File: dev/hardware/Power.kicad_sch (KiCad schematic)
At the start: 7 parts, among them J301 DC IN, Q301 IPP80P03P4L-04, U301 LF33_TO220

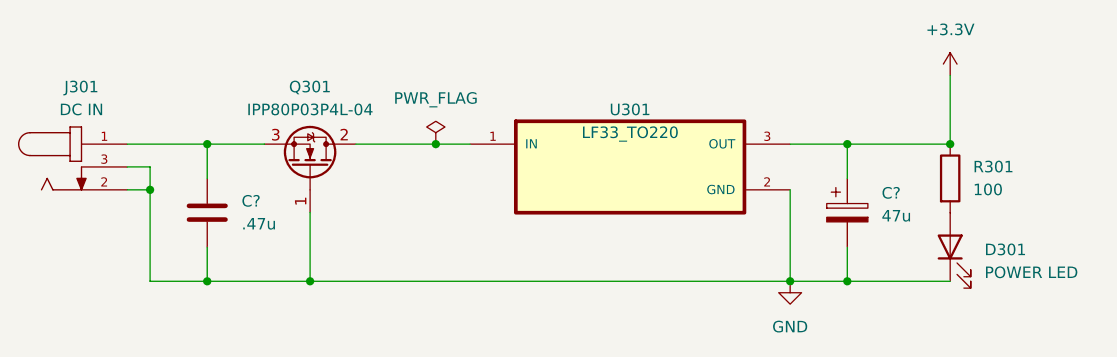
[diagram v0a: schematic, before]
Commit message: Finalized dev PCB for 1st run
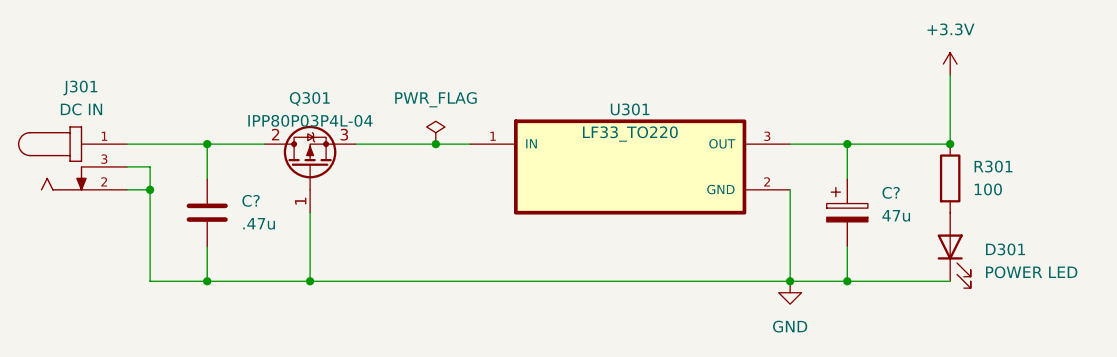
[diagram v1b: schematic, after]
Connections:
- net at C?.2, J301.1: now also Q301.2 (D); no longer Q301.3 (S)
- net at U301.1 (IN): now also Q301.3 (S); no longer Q301.2 (D)
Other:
- moved on the sheet: Q301
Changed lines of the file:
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@@
     )
   )
-  (symbol (lib_id "jcap-symbols:IPP80P03P4L-04") (at 120.65 90.17 270) (mirror x) (unit 1)
+  (symbol (lib_id "jcap-symbols:IPP80P03P4L-04") (at 120.65 91.44 90) (unit 1)
     (in_bom yes) (on_board yes) (dnp no)
-    (property "Reference" "Q301" (at 120.65 81.28 90)
+    (property "Reference" "Q301" (at 120.65 82.55 90)
       (effects (font (size 1.27 1.27)))
     )
-    (property "Value" "IPP80P03P4L-04" (at 120.65 83.82 90)
+    (property "Value" "IPP80P03P4L-04" (at 120.65 85.09 90)
       (effects (font (size 1.27 1.27)))
     )
-    (property "Footprint" "Package_TO_SOT_THT:TO-220-3_Horizontal_TabDown" (at 118.745 83.82 0)
+    (property "Footprint" "Package_TO_SOT_THT:TO-220-3_Horizontal_TabDown" (at 122.555 85.09 0)
       (effects (font (size 1.27 1.27) italic) (justify left) hide)
     )
-    (property "Datasheet" "https://www.infineon.com/dgdl/Infineon-I80P03P4L_04-DataSheet-v01_01-EN.pdf?fileId=db3a30431ddc9372011e07e95eb827d7" (at 120.65 90.17 0)
+    (property "Datasheet" "https://www.infineon.com/dgdl/Infineon-I80P03P4L_04-DataSheet-v01_01-EN.pdf?fileId=db3a30431ddc9372011e07e95eb827d7" (at 120.65 91.44 0)
       (effects (font (size 1.27 1.27)) (justify left) hide)
     )

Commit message: Finalized dev board administrivia
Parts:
- C?: Part (none) -> C330C474K5R5TA
- C?: Part (none) -> EEU-FR1J470
- D301: Part (none) -> HLMP-1790
- J301: Part (none) -> PJ-202AH
- Q301: Part (none) -> IPP80P03P4L04AKSA2
- R301: Part (none) -> CF12JT100R
- U301: value LF33_TO220 -> LM3940IT; Part (none) -> LM3940IT-3.3/NOPB
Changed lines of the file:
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@@
       (effects (font (size 1.27 1.27)) (justify bottom) hide)
     )
-    (property "Datasheet" "~" (at 95.25 90.17 0)
+    (property "Datasheet" "https://www.cuidevices.com/product/resource/pj-202ah.pdf" (at 95.25 90.17 0)
+      (effects (font (size 1.27 1.27)) hide)
+    )
+    (property "Part" "PJ-202AH" (at 95.25 90.17 0)
       (effects (font (size 1.27 1.27)) hide)
     )
@@
       (effects (font (size 1.27 1.27)) hide)
     )
-    (property "Datasheet" "~" (at 109.22 95.25 0)
+    (property "Datasheet" "https://connect.kemet.com:7667/gateway/IntelliData-ComponentDocumentation/1.0/download/datasheet/C330C474K5R5TA" (at 109.22 95.25 0)
+      (effects (font (size 1.27 1.27)) hide)
+    )
+    (property "Part" "C330C474K5R5TA" (at 109.22 95.25 0)
       (effects (font (size 1.27 1.27)) hide)
     )
@@
       (effects (font (size 1.27 1.27)))
     )
-    (property "Value" "LF33_TO220" (at 156.21 86.36 0)
+    (property "Value" "LM3940IT" (at 156.21 86.36 0)
       (effects (font (size 1.27 1.27)))
     )
@@
       (effects (font (size 1.27 1.27)) (justify bottom) hide)
     )
-    (property "Datasheet" "http://www.st.com/content/ccc/resource/technical/document/datasheet/c4/0e/7e/2a/be/bc/4c/bd/CD00000546.pdf/files/CD00000546.pdf/jcr:content/translations/en.CD00000546.pdf" (at 156.21 90.17 0)
+    (property "Datasheet" "https://www.ti.com/general/docs/suppproductinfo.tsp?distId=10&gotoUrl=https%3A%2F%2Fwww.ti.com%2Flit%2Fgpn%2Flm3940" (at 156.21 90.17 0)
+      (effects (font (size 1.27 1.27)) hide)
+    )
+    (property "Part" "LM3940IT-3.3/NOPB" (at 156.21 90.17 0)
       (effects (font (size 1.27 1.27)) hide)
     )
@@
       (effects (font (size 1.27 1.27)) (justify left) hide)
     )
+    (property "Part" "IPP80P03P4L04AKSA2" (at 120.65 91.44 90)
+      (effects (font (size 1.27 1.27)) hide)
+    )
     (pin "1")
     (pin "2")
@@
       (effects (font (size 1.27 1.27)) hide)
     )
-    (property "Datasheet" "~" (at 191.77 99.06 0)
+    (property "Datasheet" "https://mm.digikey.com/Volume0/opasdata/d220001/medias/docus/1021/HLMP-47zz,HLMP-17zz_2021-08-09.pdf" (at 191.77 99.06 0)
+      (effects (font (size 1.27 1.27)) hide)
+    )
+    (property "Part" "HLMP-1790" (at 191.77 99.06 90)
       (effects (font (size 1.27 1.27)) hide)
     )
@@
       (effects (font (size 1.27 1.27)) hide)
     )
-    (property "Datasheet" "~" (at 191.77 91.44 0)
+    (property "Datasheet" "https://www.seielect.com/catalog/sei-cf_cfm.pdf" (at 191.77 91.44 0)
+      (effects (font (size 1.27 1.27)) hide)
+    )
+    (property "Part" "CF12JT100R" (at 191.77 91.44 0)
       (effects (font (size 1.27 1.27)) hide)
     )
@@
       (effects (font (size 1.27 1.27)) hide)
     )
-    (property "Datasheet" "~" (at 180.34 95.25 0)
+    (property "Datasheet" "https://industrial.panasonic.com/cdbs/www-data/pdf/RDF0000/ABA0000C1259.pdf" (at 180.34 95.25 0)
       (effects (font (size 1.27 1.27)) hide)
     )
+    (property "Part" "EEU-FR1J470" (at 180.34 95.25 0)
+      (effects (font (size 1.27 1.27)) hide)
+    )
